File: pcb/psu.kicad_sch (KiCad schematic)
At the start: 21 parts, among them J3 3V3_JMP, U3 DC-005H-D020, U4 LMR16010

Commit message: feat: layout meterbus frontend
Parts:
- TP7: value TestPoint -> GND
- TP8: value TestPoint -> VIN
- TP9: value TestPoint -> DCDC_FB
- renumbered C7 to C10, C8 to C11, C3 to C8, C6 to C9, D7 to D10, D9 to D7, D1 to D8, D8 to D9, F1 to F3, J3 to J1, L3 to L1, R4 to R11, R8 to R12, R11 to R13, R12 to R14, U3 to U4, U4 to U5
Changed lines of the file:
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@@
 		(dnp no)
 		(fields_autoplaced yes)
-		(property "Reference" "#PWR028"
+		(property "Reference" "#PWR029"
 			(at 187.96 95.25 0)
 			(hide yes)
@@
 			(project "EveningStar"
 				(path "/4c61f5a2-f8d4-462a-9bc3-d74437d30372/2e538fbd-4766-4d3c-804f-b602af6e3385"
-					(reference "#PWR028")
+					(reference "#PWR029")
 					(unit 1)
 				)
@@
 		(dnp no)
 		(fields_autoplaced yes)
-		(property "Reference" "#PWR029"
+		(property "Reference" "#PWR030"
 			(at 199.39 74.93 0)
 			(hide yes)
@@
 			(project "EveningStar"
 				(path "/4c61f5a2-f8d4-462a-9bc3-d74437d30372/2e538fbd-4766-4d3c-804f-b602af6e3385"
-					(reference "#PWR029")
+					(reference "#PWR030")
 					(unit 1)
 				)
@@
 		(dnp no)
 		(fields_autoplaced yes)
-		(property "Reference" "D8"
+		(property "Reference" "D9"
 			(at 86.615 45.72 0)
 			(show_name no)
@@
 			(project "EveningStar"
 				(path "/4c61f5a2-f8d4-462a-9bc3-d74437d30372/2e538fbd-4766-4d3c-804f-b602af6e3385"
-					(reference "D8")
+					(reference "D9")
 					(unit 1)
 				)
@@
 		(dnp no)
 		(fields_autoplaced yes)
-		(property "Reference" "R12"
+		(property "Reference" "R14"
 			(at 190.5 81.2799 90)
 			(show_name no)
@@
 			(project "EveningStar"
 				(path "/4c61f5a2-f8d4-462a-9bc3-d74437d30372/2e538fbd-4766-4d3c-804f-b602af6e3385"
-					(reference "R12")
+					(reference "R14")
 					(unit 1)
 				)
@@
 		(dnp no)
 		(fields_autoplaced yes)
-		(property "Reference" "#PWR026"
+		(property "Reference" "#PWR027"
 			(at 128.27 105.41 0)
 			(hide yes)
@@
 			(project "EveningStar"
 				(path "/4c61f5a2-f8d4-462a-9bc3-d74437d30372/2e538fbd-4766-4d3c-804f-b602af6e3385"
-					(reference "#PWR026")
+					(reference "#PWR027")
 					(unit 1)
 				)
@@
 			)
 		)
-		(property "Value" "TestPoint"
+		(property "Value" "GND"
 			(at 78.74 68.0719 0)
 			(show_name no)
@@
 		(dnp no)
 		(fields_autoplaced yes)
-		(property "Reference" "C3"
+		(property "Reference" "C8"
 			(at 110.49 54.6099 0)
 			(show_name no)
@@
 			(project "EveningStar"
 				(path "/4c61f5a2-f8d4-462a-9bc3-d74437d30372/2e538fbd-4766-4d3c-804f-b602af6e3385"
-					(reference "C3")
+					(reference "C8")
 					(unit 1)
 				)
@@
 		(dnp no)
 		(fields_autoplaced yes)
-		(property "Reference" "D9"
+		(property "Reference" "D7"
 			(at 80.01 55.8799 0)
 			(show_name no)
@@
 			(project "EveningStar"
 				(path "/4c61f5a2-f8d4-462a-9bc3-d74437d30372/2e538fbd-4766-4d3c-804f-b602af6e3385"
-					(reference "D9")
+					(reference "D7")
 					(unit 1)
 				)
@@
 		(dnp no)
 		(fields_autoplaced yes)
-		(property "Reference" "U4"
+		(property "Reference" "U5"
 			(at 143.51 44.45 0)
 			(show_name no)
@@
 			(project "EveningStar"
 				(path "/4c61f5a2-f8d4-462a-9bc3-d74437d30372/2e538fbd-4766-4d3c-804f-b602af6e3385"
-					(reference "U4")
+					(reference "U5")
 					(unit 1)
 				)
@@
 		(dnp no)
 		(fields_autoplaced yes)
-		(property "Reference" "#PWR023"
+		(property "Reference" "#PWR024"
 			(at 67.31 69.85 0)
 			(hide yes)
@@
 			(project "EveningStar"
 				(path "/4c61f5a2-f8d4-462a-9bc3-d74437d30372/2e538fbd-4766-4d3c-804f-b602af6e3385"
-					(reference "#PWR023")
+					(reference "#PWR024")
 					(unit 1)
 				)
@@
 		(dnp no)
 		(fields_autoplaced yes)
-		(property "Reference" "#PWR030"
+		(property "Reference" "#PWR031"
 			(at 251.46 60.96 0)
 			(hide yes)
@@
 			(project "EveningStar"
 				(path "/4c61f5a2-f8d4-462a-9bc3-d74437d30372/2e538fbd-4766-4d3c-804f-b602af6e3385"
-					(reference "#PWR030")
+					(reference "#PWR031")
 					(unit 1)
 				)
@@
 		(dnp no)
 		(fields_autoplaced yes)
-		(property "Reference" "R11"
+		(property "Reference" "R13"
 			(at 190.5 63.4999 0)
 			(show_name no)
@@
 			(project "EveningStar"
 				(path "/4c61f5a2-f8d4-462a-9bc3-d74437d30372/2e538fbd-4766-4d3c-804f-b602af6e3385"
-					(reference "R11")
+					(reference "R13")
 					(unit 1)
 				)
@@
 		(dnp no)
 		(fields_autoplaced yes)
-		(property "Reference" "D7"
+		(property "Reference" "D10"
 			(at 171.45 63.2449 90)
 			(show_name no)
@@
 			(project "EveningStar"
 				(path "/4c61f5a2-f8d4-462a-9bc3-d74437d30372/2e538fbd-4766-4d3c-804f-b602af6e3385"
-					(reference "D7")
+					(reference "D10")
 					(unit 1)
 				)
@@
 		(dnp no)
 		(fields_autoplaced yes)
-		(property "Reference" "C7"
+		(property "Reference" "C10"
 			(at 162.56 43.18 90)
 			(show_name no)
@@
 			(project "EveningStar"
 				(path "/4c61f5a2-f8d4-462a-9bc3-d74437d30372/2e538fbd-4766-4d3c-804f-b602af6e3385"
-					(reference "C7")
+					(reference "C10")
 					(unit 1)
 				)
@@
 		(dnp no)
 		(fields_autoplaced yes)
-		(property "Reference" "F1"
+		(property "Reference" "F3"
 			(at 69.85 45.72 0)
 			(show_name no)
@@
 			(project "EveningStar"
 				(path "/4c61f5a2-f8d4-462a-9bc3-d74437d30372/2e538fbd-4766-4d3c-804f-b602af6e3385"
-					(reference "F1")
+					(reference "F3")
 					(unit 1)
 				)
@@
 		(dnp no)
 		(fields_autoplaced yes)
-		(property "Reference" "#PWR024"
+		(property "Reference" "#PWR025"
 			(at 107.95 69.85 0)
 			(hide yes)
@@
 			(project "EveningStar"
 				(path "/4c61f5a2-f8d4-462a-9bc3-d74437d30372/2e538fbd-4766-4d3c-804f-b602af6e3385"
-					(reference "#PWR024")
+					(reference "#PWR025")
 					(unit 1)
 				)
@@
 		(dnp no)
 		(fields_autoplaced yes)
-		(property "Reference" "J3"
+		(property "Reference" "J1"
 			(at 218.44 51.4349 90)
 			(show_name no)
@@
 			(project "EveningStar"
 				(path "/4c61f5a2-f8d4-462a-9bc3-d74437d30372/2e538fbd-4766-4d3c-804f-b602af6e3385"
-					(reference "J3")
+					(reference "J1")
 					(unit 1)
 				)
@@
 			)
 		)
-		(property "Value" "TestPoint"
+		(property "Value" "VIN"
 			(at 110.49 48.7679 0)
 			(show_name no)
@@
 		(in_pos_files yes)
 		(dnp no)
-		(property "Reference" "R8"
+		(property "Reference" "R12"
 			(at 125.73 92.7099 90)
 			(show_name no)
@@
 			(project "EveningStar"
 				(path "/4c61f5a2-f8d4-462a-9bc3-d74437d30372/2e538fbd-4766-4d3c-804f-b602af6e3385"
-					(reference "R8")
+					(reference "R12")
 					(unit 1)
 				)
@@
 		(dnp no)
 		(fields_autoplaced yes)
-		(property "Reference" "D1"
+		(property "Reference" "D8"
 			(at 86.615 31.75 0)
 			(show_name no)
@@
 			(project "EveningStar"
 				(path "/4c61f5a2-f8d4-462a-9bc3-d74437d30372/2e538fbd-4766-4d3c-804f-b602af6e3385"
-					(reference "D1")
+					(reference "D8")
 					(unit 1)
 				)
@@
 		(dnp no)
 		(fields_autoplaced yes)
-		(property "Reference" "L3"
+		(property "Reference" "L1"
 			(at 177.77 52.07 0)
 			(show_name no)
@@
 			(project "EveningStar"
 				(path "/4c61f5a2-f8d4-462a-9bc3-d74437d30372/2e538fbd-4766-4d3c-804f-b602af6e3385"
-					(reference "L3")
+					(reference "L1")
 					(unit 1)
 				)
@@
 		(dnp no)
 		(fields_autoplaced yes)
-		(property "Reference" "U3"
+		(property "Reference" "U4"
 			(at 51.435 46.99 0)
 			(show_name no)
@@
 			(project "EveningStar"
 				(path "/4c61f5a2-f8d4-462a-9bc3-d74437d30372/2e538fbd-4766-4d3c-804f-b602af6e3385"
-					(reference "U3")
+					(reference "U4")
 					(unit 1)
 				)
@@
 			)
 		)
-		(property "Value" "TestPoint"
+		(property "Value" "DCDC_FB"
 			(at 176.53 74.1679 0)
 			(show_name no)
@@
 		(dnp no)
 		(fields_autoplaced yes)
-		(property "Reference" "#FLG06"
+		(property "Reference" "#FLG05"
 			(at 241.3 55.245 0)
 			(hide yes)
@@
 			(project "EveningStar"
 				(path "/4c61f5a2-f8d4-462a-9bc3-d74437d30372/2e538fbd-4766-4d3c-804f-b602af6e3385"
-					(reference "#FLG06")
+					(reference "#FLG05")
 					(unit 1)
 				)
@@
 		(dnp no)
 		(fields_autoplaced yes)
-		(property "Reference" "#PWR025"
+		(property "Reference" "#PWR026"
 			(at 128.27 71.12 0)
 			(hide yes)
@@
 			(project "EveningStar"
 				(path "/4c61f5a2-f8d4-462a-9bc3-d74437d30372/2e538fbd-4766-4d3c-804f-b602af6e3385"
-					(reference "#PWR025")
+					(reference "#PWR026")
 					(unit 1)
 				)
@@
 		(in_pos_files yes)
 		(dnp no)
-		(property "Reference" "R4"
+		(property "Reference" "R11"
 			(at 125.73 72.3899 0)
 			(show_name no)
@@
 			(project "EveningStar"
 				(path "/4c61f5a2-f8d4-462a-9bc3-d74437d30372/2e538fbd-4766-4d3c-804f-b602af6e3385"
-					(reference "R4")
+					(reference "R11")
 					(unit 1)
 				)
@@
 		(dnp no)
 		(fields_autoplaced yes)
-		(property "Reference" "#PWR027"
+		(property "Reference" "#PWR028"
 			(at 167.64 76.2 0)
 			(hide yes)
@@
 			(project "EveningStar"
 				(path "/4c61f5a2-f8d4-462a-9bc3-d74437d30372/2e538fbd-4766-4d3c-804f-b602af6e3385"
-					(reference "#PWR027")
+					(reference "#PWR028")
 					(unit 1)
 				)
@@
 		(dnp no)
 		(fields_autoplaced yes)
-		(property "Reference" "C6"
+		(property "Reference" "C9"
 			(at 123.19 54.6099 0)
 			(show_name no)
@@
 			(project "EveningStar"
 				(path "/4c61f5a2-f8d4-462a-9bc3-d74437d30372/2e538fbd-4766-4d3c-804f-b602af6e3385"
-					(reference "C6")
+					(reference "C9")
 					(unit 1)
 				)
@@
 		(dnp no)
 		(fields_autoplaced yes)
-		(property "Reference" "C8"
+		(property "Reference" "C11"
 			(at 201.93 60.9599 0)
 			(show_name no)
@@
 			(project "EveningStar"
 				(path "/4c61f5a2-f8d4-462a-9bc3-d74437d30372/2e538fbd-4766-4d3c-804f-b602af6e3385"
-					(reference "C8")
+					(reference "C11")
 					(unit 1)
 				)

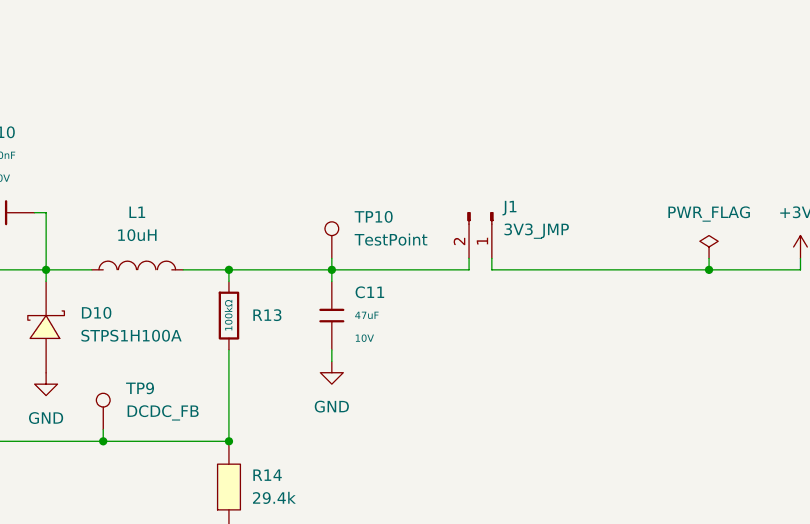
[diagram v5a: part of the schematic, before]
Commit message: feat: roughly lay out mcu
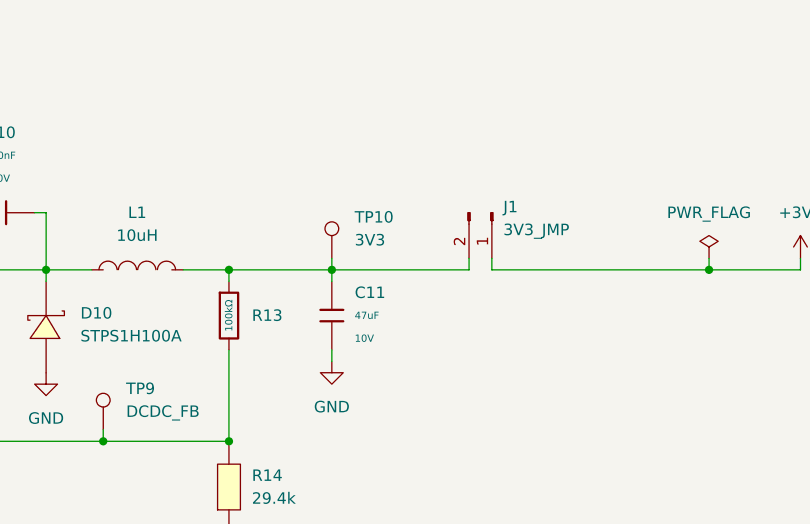
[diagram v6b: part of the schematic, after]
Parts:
- TP10: value TestPoint -> 3V3
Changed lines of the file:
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@@
 			)
 		)
-		(property "Value" "TestPoint"
+		(property "Value" "3V3"
 			(at 201.93 55.1179 0)
 			(show_name no)

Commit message: feat: layout psu and rest of mcu
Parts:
- removed R11: 10kΩ, PCM_JLCPCB:R_0603, symbol PCM_JLCPCB-Resistors:0603,10kΩ
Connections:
- no-connect marks 1 -> 2

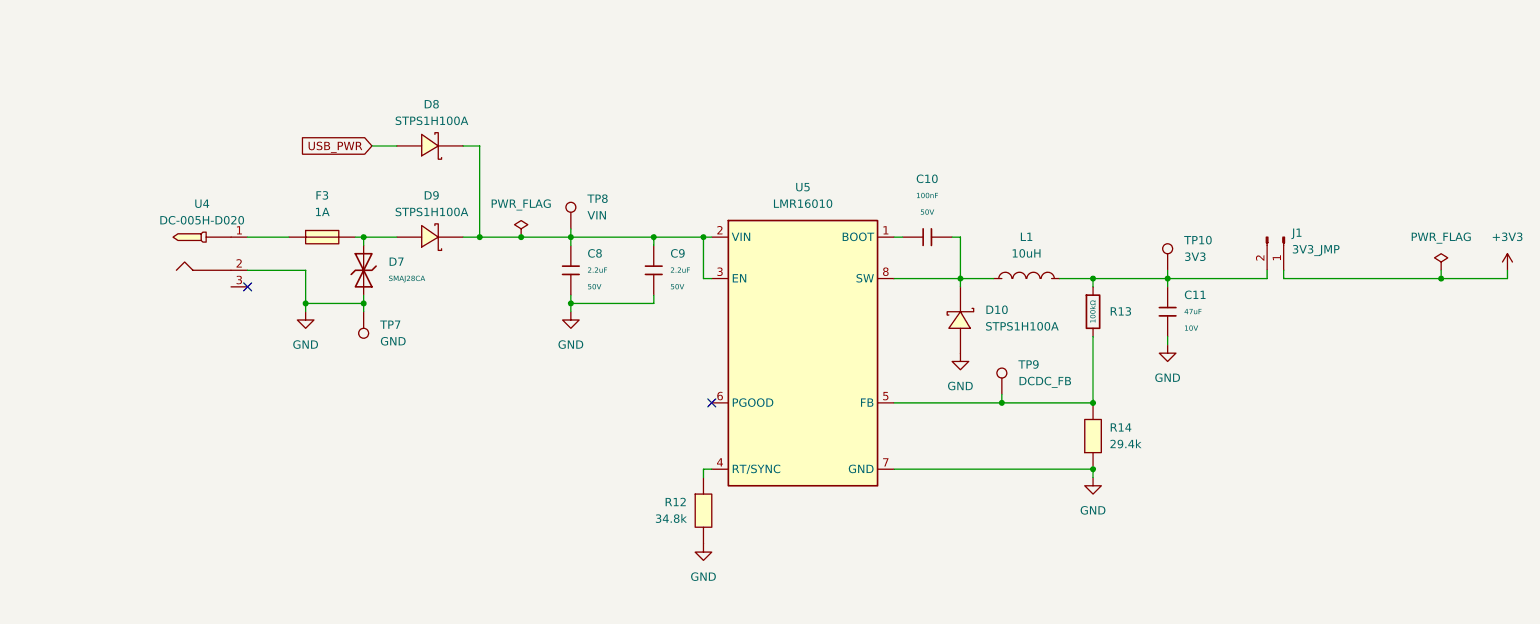
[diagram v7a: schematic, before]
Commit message: feat: create pcb production files and swap some parts for basic
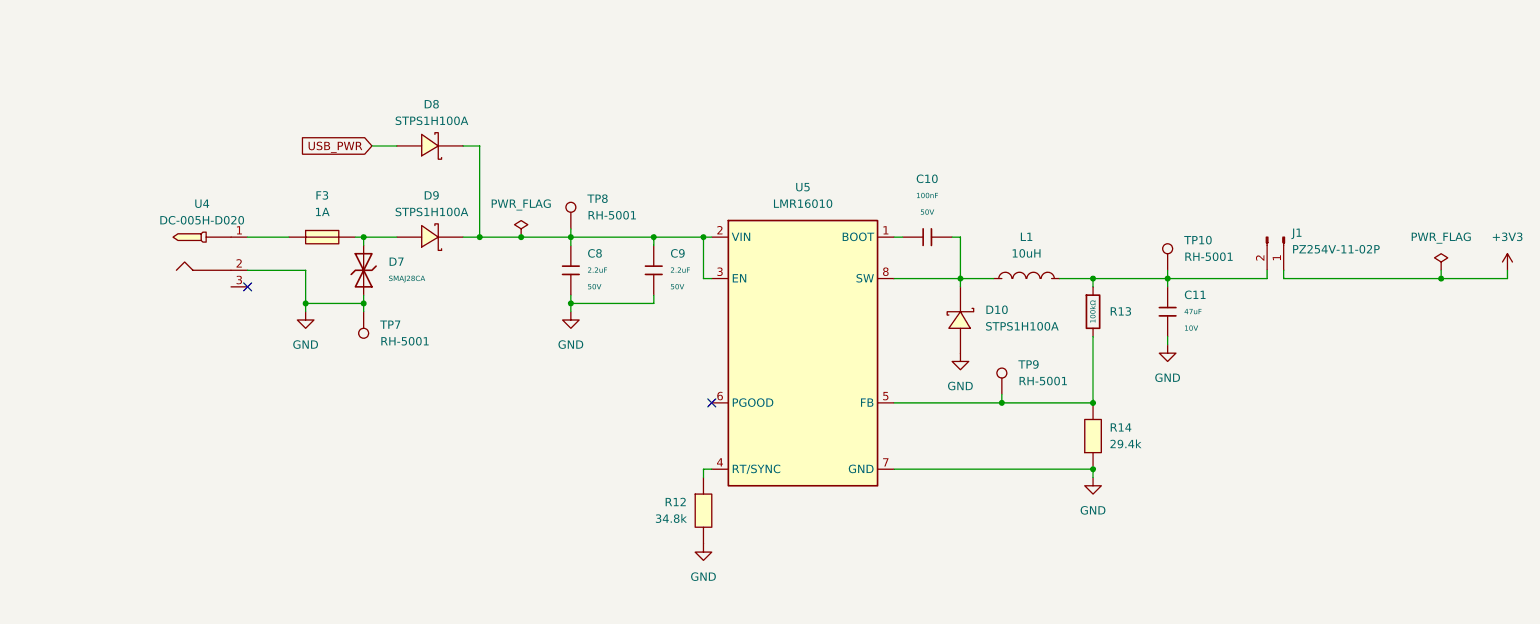
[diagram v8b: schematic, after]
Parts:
- J1: value 3V3_JMP -> PZ254V-11-02P
- TP10: value 3V3 -> RH-5001
- TP7: value GND -> RH-5001
- TP8: value VIN -> RH-5001
- TP9: value DCDC_FB -> RH-5001
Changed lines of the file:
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@@
 			)
 		)
-		(property "Value" "GND"
+		(property "Value" "RH-5001"
 			(at 78.74 68.0719 0)
 			(show_name no)
@@
 			)
 		)
-		(property "Description" "test point"
+		(property "Description" "GND"
 			(at 76.2 63.5 0)
 			(hide yes)
@@
 			)
 		)
-		(property "Value" "3V3_JMP"
+		(property "Value" "PZ254V-11-02P"
 			(at 218.44 53.9749 90)
 			(show_name no)
@@
 			)
 		)
-		(property "Description" "Generic connector, single row, 01x02, script generated"
+		(property "Description" "3V3_JMP"
 			(at 217.17 52.07 0)
 			(hide yes)
@@
 			)
 		)
-		(property "Value" "VIN"
+		(property "Value" "RH-5001"
 			(at 110.49 48.7679 0)
 			(show_name no)
@@
 			)
 		)
-		(property "Description" "test point"
+		(property "Description" "VIN"
 			(at 107.95 50.8 0)
 			(hide yes)
@@
 			)
 		)
-		(property "Value" "3V3"
+		(property "Value" "RH-5001"
 			(at 201.93 55.1179 0)
 			(show_name no)
@@
 			)
 		)
-		(property "Description" "test point"
+		(property "Description" "3V3"
 			(at 199.39 57.15 0)
 			(hide yes)
@@
 			)
 		)
-		(property "Value" "DCDC_FB"
+		(property "Value" "RH-5001"
 			(at 176.53 74.1679 0)
 			(show_name no)
@@
 			)
 		)
-		(property "Description" "test point"
+		(property "Description" "DCDC_FB"
 			(at 173.99 76.2 0)
 			(hide yes)
